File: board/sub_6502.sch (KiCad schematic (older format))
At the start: 0 parts

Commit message: More progress on the schematic. 6502 Done.
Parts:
- added C301: 0.1u, symbol Device:C
- added C302: 10u, symbol Device:C
- added C? (x4): 1u, symbol Device:C
- added JP301: Jumper_NC_Small, symbol Device:Jumper_NC_Small
- added JP302: WireJumper, symbol Device:Jumper_NC_Small
- added Q301: Q_NPN_BEC, symbol Device:Q_NPN_BEC
- added R302: 1k, symbol Device:R
- added R303, R304, R305: 4.7k, symbol Device:R
- added U301, U302, U303, U305: 74HCT245, symbol Logic_74xx:74HC245
- added U304: 6502, symbol quokka:6502
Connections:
- new net: JP301.2, JP302.2, U304.1 (GND/(~VP~))
- new net: Q301.3 (C), R303.2, U304.2 (RDY)
- new net: R305.1, U304.36 ((BE))
- new net: R304.1, U304.5 ((~ML~))
- new net: Q301.1 (B), R302.1
- new net +5V: C301.1, C302.1, C?.1, C?.1, C?.1, C?.1, R303.1, U301.20 (VCC), U302.20 (VCC), U303.20 (VCC), U304.8 (VCC), U305.20 (VCC)
- new net 6502_PHI0: U304.37 (PHI0)
- new net 6502_PHI1: U301.2 (A0)
- new net 6502_PHI2: U301.3 (A1)
- new net 6502_RDY: R302.2
- new net 6502_R~W: U301.5 (A3)
- new net 6502_SO: U304.38 (~SO)
- new net 6502_SYNC: U301.4 (A2)
- new net 6502_~IRQ: U304.4 (~IRQ)
- new net 6502_~NMI: U304.6 (~NMI)
- new net 6502_~RES: U304.40 (~RES)
- new net A0: U302.18 (B0), U302.2 (A0), U304.9 (A0)
- new net A1: U302.17 (B1), U302.3 (A1), U304.10 (A1)
- new net A10: U303.16 (B2), U303.4 (A2), U304.19 (A10)
- new net A11: U303.15 (B3), U303.5 (A3), U304.20 (A11)
- new net A12: U303.14 (B4), U303.6 (A4), U304.22 (A12)
- new net A13: U303.13 (B5), U303.7 (A5), U304.23 (A13)
- new net A14: U303.12 (B6), U303.8 (A6), U304.24 (A14)
- new net A15: U303.11 (B7), U303.9 (A7), U304.25 (A15)
- new net A2: U302.16 (B2), U302.4 (A2), U304.11 (A2)
- new net A3: U302.15 (B3), U302.5 (A3), U304.12 (A3)
- new net A4: U302.14 (B4), U302.6 (A4), U304.13 (A4)
- new net A5: U302.13 (B5), U302.7 (A5), U304.14 (A5)
- new net A6: U302.12 (B6), U302.8 (A6), U304.15 (A6)
- new net A7: U302.11 (B7), U302.9 (A7), U304.16 (A7)
- new net A8: U303.18 (B0), U303.2 (A0), U304.17 (A8)
- new net A9: U303.17 (B1), U303.3 (A1), U304.18 (A9)
- new net D0: U304.33 (D0), U305.18 (B0), U305.2 (A0)
- new net D1: U304.32 (D1), U305.17 (B1), U305.3 (A1)
- new net D2: U304.31 (D2), U305.16 (B2), U305.4 (A2)
- new net D3: U304.30 (D3), U305.15 (B3), U305.5 (A3)
- new net D4: U304.29 (D4), U305.14 (B4), U305.6 (A4)
- new net D5: U304.28 (D5), U305.13 (B5), U305.7 (A5)
- new net D6: U304.27 (D6), U305.12 (B6), U305.8 (A6)
- new net D7: U304.26 (D7), U305.11 (B7), U305.9 (A7)
- new net GND: C301.2, C302.2, C?.2, C?.2, C?.2, C?.2, JP301.1, JP302.1, Q301.2 (E), R304.2, R305.2, U301.1 (A->B), U301.10 (GND), U302.1 (A->B), U302.10 (GND), U303.1 (A->B), U303.10 (GND), U304.21 (GND), U305.10 (GND)
- new net PHI1: U301.18 (B0), U304.3 (PHI1out)
- new net PHI2: U301.17 (B1), U304.39 (PHI2out)
- new net R~W: U301.15 (B3), U304.34 (R/~W), U305.1 (A->B)
- new net SYNC: U301.16 (B2), U304.7 (SYNC)
- new net ~BusEnable: U301.19 (CE), U302.19 (CE), U303.19 (CE), U305.19 (CE)
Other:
- note added: "Note: Some 6502s have\na bidirectional RDY while\nothers are just inputs."
- note added: "Open for W65C02\nClose for all others"

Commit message: More schematic progress
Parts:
- gave numbers to parts that had none: 4
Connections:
- net GND: now also U301.11 (B7), U301.12 (B6), U301.13 (B5), U301.14 (B4)
- no-connect marks 0 -> 4
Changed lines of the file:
@@
 	8300 1200 8300 1300
 $Comp
-L Device:C C?
+L Device:C C1002
 U 1 1 5ACC7CA4
 P 6200 2350
-F 0 "C?" H 6315 2396 50  0000 L CNN
+F 0 "C1002" H 6315 2396 50  0000 L CNN
 F 1 "1u" H 6315 2305 50  0000 L CNN
 F 2 "" H 6238 2200 50  0001 C CNN
@@
 $EndComp
 $Comp
-L power:GND #PWR?
+L power:GND #PWR01004
 U 1 1 5ACC7CAA
 P 6200 2500
-F 0 "#PWR?" H 6200 2250 50  0001 C CNN
+F 0 "#PWR01004" H 6200 2250 50  0001 C CNN
 F 1 "GND" H 6205 2327 50  0000 C CNN
 F 2 "" H 6200 2500 50  0001 C CNN
@@
 $EndComp
 $Comp
-L power:+5V #PWR?
+L power:+5V #PWR01003
 U 1 1 5ACCE535
 P 6200 2200
-F 0 "#PWR?" H 6200 2050 50  0001 C CNN
+F 0 "#PWR01003" H 6200 2050 50  0001 C CNN
 F 1 "+5V" H 6215 2373 50  0000 C CNN
 F 2 "" H 6200 2200 50  0001 C CNN
@@
 $EndComp
 $Comp
-L Device:C C?
+L Device:C C1001
 U 1 1 5ACE23C8
 P 4300 5000
-F 0 "C?" H 4415 5046 50  0000 L CNN
+F 0 "C1001" H 4415 5046 50  0000 L CNN
 F 1 "1u" H 4415 4955 50  0000 L CNN
 F 2 "" H 4338 4850 50  0001 C CNN
@@
 $EndComp
 $Comp
-L power:GND #PWR?
+L power:GND #PWR01002
 U 1 1 5ACE23CE
 P 4300 5150
-F 0 "#PWR?" H 4300 4900 50  0001 C CNN
+F 0 "#PWR01002" H 4300 4900 50  0001 C CNN
 F 1 "GND" H 4305 4977 50  0000 C CNN
 F 2 "" H 4300 5150 50  0001 C CNN
@@
 $EndComp
 $Comp
-L power:+5V #PWR?
+L power:+5V #PWR01001
 U 1 1 5ACE23D4
 P 4300 4850
-F 0 "#PWR?" H 4300 4700 50  0001 C CNN
+F 0 "#PWR01001" H 4300 4700 50  0001 C CNN
 F 1 "+5V" H 4315 5023 50  0000 C CNN
 F 2 "" H 4300 4850 50  0001 C CNN
@@
 $EndComp
 $Comp
-L Device:C C?
+L Device:C C1003
 U 1 1 5ACEF717
 P 7800 5000
-F 0 "C?" H 7915 5046 50  0000 L CNN
+F 0 "C1003" H 7915 5046 50  0000 L CNN
 F 1 "1u" H 7915 4955 50  0000 L CNN
 F 2 "" H 7838 4850 50  0001 C CNN
@@
 $EndComp
 $Comp
-L power:GND #PWR?
+L power:GND #PWR01006
 U 1 1 5ACEF71D
 P 7800 5150
-F 0 "#PWR?" H 7800 4900 50  0001 C CNN
+F 0 "#PWR01006" H 7800 4900 50  0001 C CNN
 F 1 "GND" H 7805 4977 50  0000 C CNN
 F 2 "" H 7800 5150 50  0001 C CNN
@@
 $EndComp
 $Comp
-L power:+5V #PWR?
+L power:+5V #PWR01005
 U 1 1 5ACEF723
 P 7800 4850
-F 0 "#PWR?" H 7800 4700 50  0001 C CNN
+F 0 "#PWR01005" H 7800 4700 50  0001 C CNN
 F 1 "+5V" H 7815 5023 50  0000 C CNN
 F 2 "" H 7800 4850 50  0001 C CNN
@@
 $EndComp
 $Comp
-L Device:C C?
+L Device:C C1004
 U 1 1 5ACFCC74
 P 10250 5000
-F 0 "C?" H 10365 5046 50  0000 L CNN
+F 0 "C1004" H 10365 5046 50  0000 L CNN
 F 1 "1u" H 10365 4955 50  0000 L CNN
 F 2 "" H 10288 4850 50  0001 C CNN
@@
 $EndComp
 $Comp
-L power:GND #PWR?
+L power:GND #PWR01008
 U 1 1 5ACFCC7A
 P 10250 5150
-F 0 "#PWR?" H 10250 4900 50  0001 C CNN
+F 0 "#PWR01008" H 10250 4900 50  0001 C CNN
 F 1 "GND" H 10255 4977 50  0000 C CNN
 F 2 "" H 10250 5150 50  0001 C CNN
@@
 $EndComp
 $Comp
-L power:+5V #PWR?
+L power:+5V #PWR01007
 U 1 1 5ACFCC80
 P 10250 4850
-F 0 "#PWR?" H 10250 4700 50  0001 C CNN
+F 0 "#PWR01007" H 10250 4700 50  0001 C CNN
 F 1 "+5V" H 10265 5023 50  0000 C CNN
 F 2 "" H 10250 4850 50  0001 C CNN
@@
 	1    0    0    -1
 $EndComp
+NoConn ~ 4800 2250
+NoConn ~ 4800 2350
+NoConn ~ 4800 2450
+NoConn ~ 4800 2550
+$Comp
+L power:GND #PWR0101
+U 1 1 5AD8E0AD
+P 5900 2650
+F 0 "#PWR0101" H 5900 2400 50  0001 C CNN
+F 1 "GND" H 5905 2477 50  0000 C CNN
+F 2 "" H 5900 2650 50  0001 C CNN
+F 3 "" H 5900 2650 50  0001 C CNN
+	1    5900 2650
+	1    0    0    -1
+$EndComp
+Wire Wire Line
+	5800 2250 5900 2250
+Wire Wire Line
+	5900 2250 5900 2350
+Wire Wire Line
+	5800 2550 5900 2550
+Connection ~ 5900 2550
+Wire Wire Line
+	5900 2550 5900 2650
+Wire Wire Line
+	5800 2450 5900 2450
+Connection ~ 5900 2450
+Wire Wire Line
+	5900 2450 5900 2550
+Wire Wire Line
+	5800 2350 5900 2350
 Wire Bus Line
 	9950 3200 9950 3850
@@
 Wire Bus Line
 	10050 2200 10050 5100
+Connection ~ 5900 2350
+Wire Wire Line
+	5900 2350 5900 2450
 $EndSCHEMATC

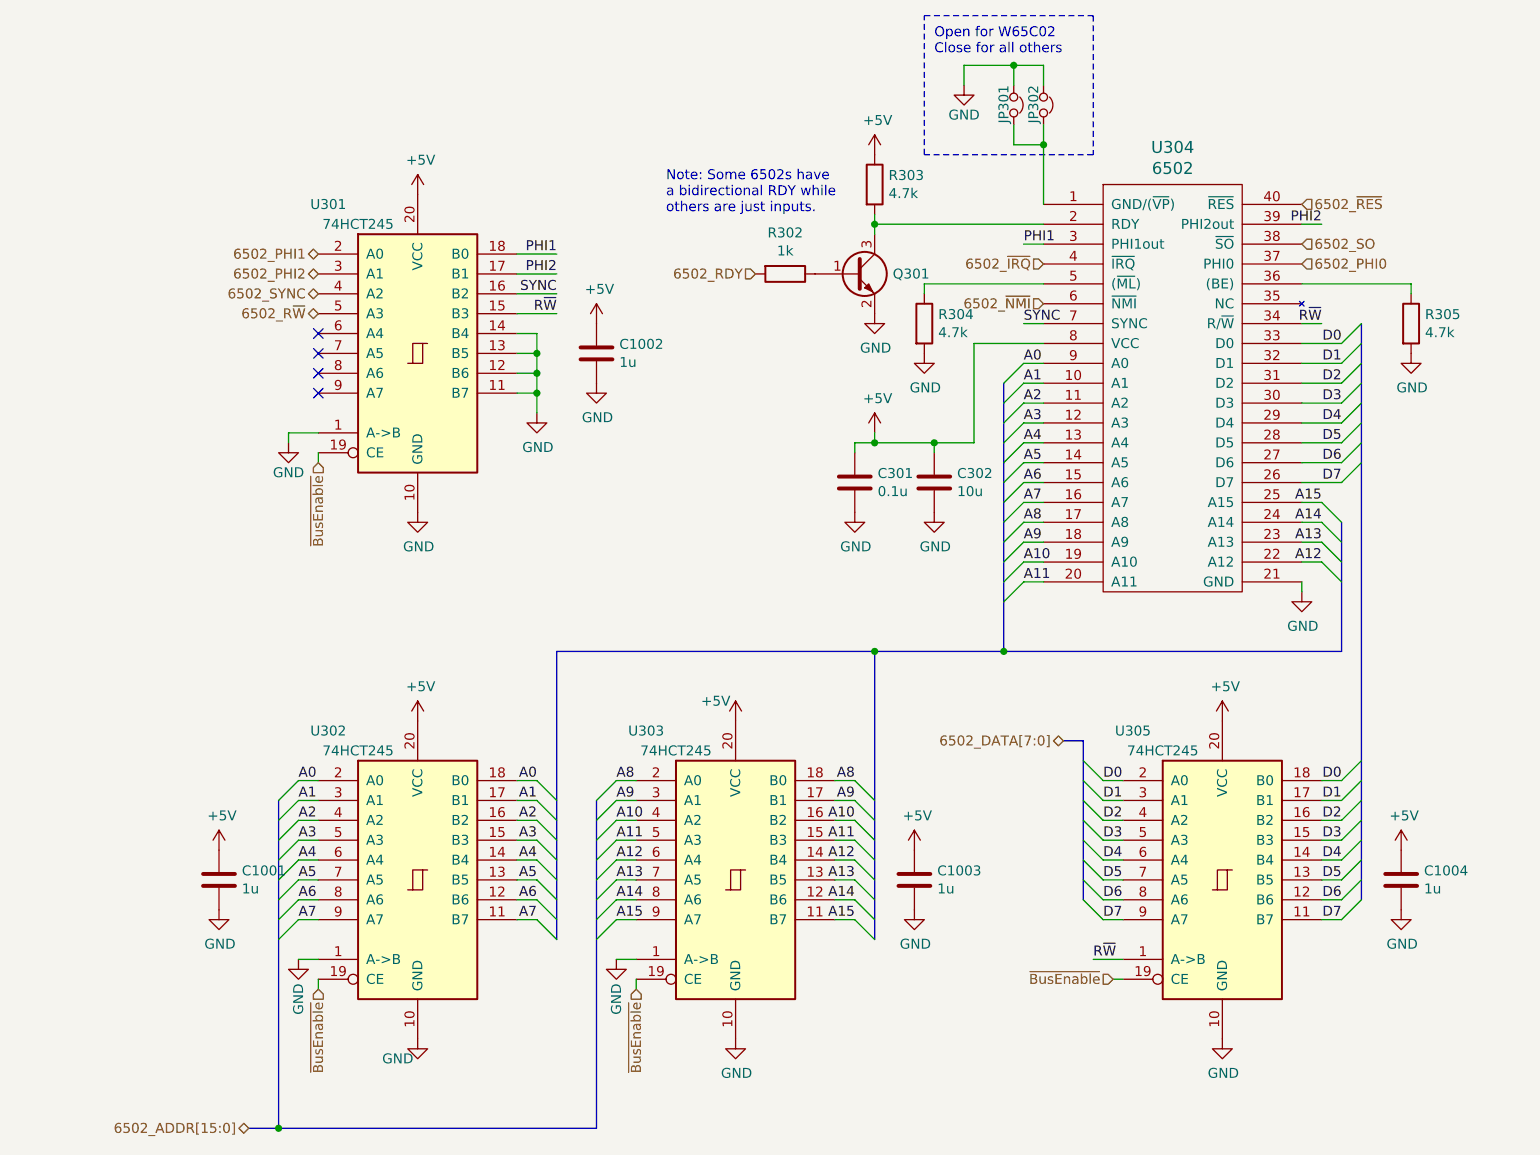
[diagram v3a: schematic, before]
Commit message: Level converters complete, display almost done
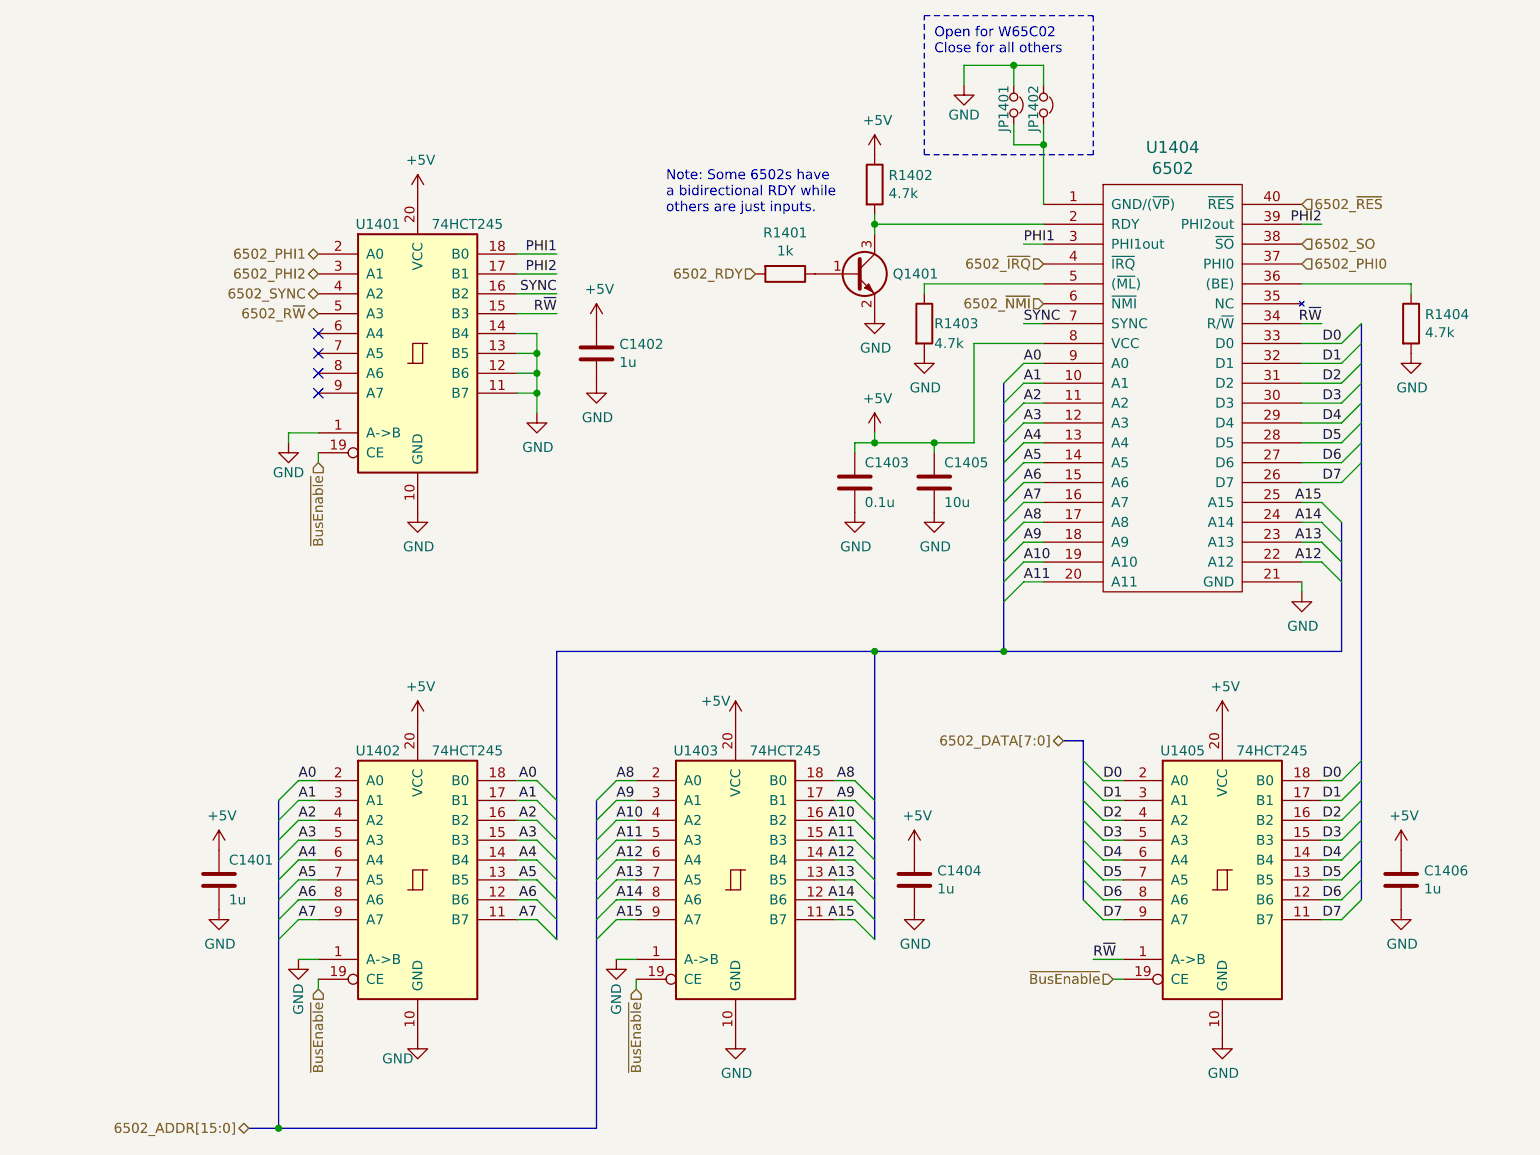
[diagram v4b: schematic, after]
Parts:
- renumbered C1001 to C1401, C1002 to C1402, C301 to C1403, C1003 to C1404, C302 to C1405, C1004 to C1406, JP301 to JP1401, JP302 to JP1402, Q301 to Q1401, R302 to R1401, R303 to R1402, R304 to R1403, R305 to R1404, U301 to U1401, U302 to U1402, U303 to U1403, U304 to U1404, U305 to U1405

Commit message: More Schematic progress
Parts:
- renumbered C1401 to C1201, C1402 to C1202, C1403 to C1203, C1404 to C1204, C1405 to C1205, C1406 to C1206, JP1401 to JP1201, JP1402 to JP1202, Q1401 to Q1201, R1401 to R1201, R1402 to R1202, R1403 to R1203, R1404 to R1204, U1401 to U1201, U1402 to U1202, U1403 to U1203, U1404 to U1204, U1405 to U1205
